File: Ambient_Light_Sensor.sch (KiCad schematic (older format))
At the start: 7 parts, among them U2001 OPT3001

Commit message: Resolved an issue with the field names of resistors on anode and grid driver sheets
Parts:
- R2004, R2005: value 100 -> 0
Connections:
- wire segments 6 -> 8
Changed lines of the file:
@@
 P 7230 3650
 F 0 "R2004" V 7630 3650 50  0000 C CNN
-F 1 "100" V 7230 3650 50  0000 C CNN
+F 1 "0" V 7230 3650 50  0000 C CNN
 F 2 "Resistors_SMD:R_0603" H 7230 3650 50  0001 C CNN
 F 3 "" H 7230 3650 50  0001 C CNN
@@
 P 7230 3750
 F 0 "R2005" V 7630 3750 50  0000 C CNN
-F 1 "100" V 7230 3750 50  0000 C CNN
+F 1 "0" V 7230 3750 50  0000 C CNN
 F 2 "Resistors_SMD:R_0603" H 7230 3750 50  0001 C CNN
 F 3 "" H 7230 3750 50  0001 C CNN
@@
 $EndComp
 Wire Wire Line
-	7080 3650 4450 3650
+	7080 3650 5640 3650
 Wire Wire Line
-	7080 3750 4450 3750
+	7080 3750 6260 3750
 $Comp
 L Custom-Library:+3.3V #PWR2003
@@
 	1    0    0    -1
 $EndComp
+Wire Wire Line
+	6260 3750 4450 3750
+Wire Wire Line
+	5640 3650 4450 3650
 $EndSCHEMATC

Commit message: Added a config field for every part, DNP some I2C pullups, added I2C header, changed some serial port functionality
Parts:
- R2002, R2003: Config (none) -> DNP
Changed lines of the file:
@@
 F 2 "Resistors_SMD:R_0603" H 6260 3350 50  0001 C CNN
 F 3 "" H 6260 3350 50  0001 C CNN
-F 4 "0603" H 6340 3430 50  0000 L CNN "display_footprint"
-F 5 "1%" H 6340 3350 50  0000 L CNN "Tolerance"
-F 6 "1/10W" H 6350 3270 50  0000 L CNN "Wattage"
-F 7 "A102203CT-ND" H 6560 3750 60  0001 C CNN "Digi-Key PN"
+F 4 "DNP" H 6340 3500 50  0000 L CNN "Config"
+F 5 "0603" H 6340 3430 50  0000 L CNN "display_footprint"
+F 6 "1%" H 6340 3350 50  0000 L CNN "Tolerance"
+F 7 "1/10W" H 6350 3270 50  0000 L CNN "Wattage"
+F 8 "A102203CT-ND" H 6560 3750 60  0001 C CNN "Digi-Key PN"
 	1    6260 3350
 	-1   0    0    -1
@@
 F 2 "Resistors_SMD:R_0603" H 5640 3350 50  0001 C CNN
 F 3 "" H 5640 3350 50  0001 C CNN
-F 4 "0603" H 5720 3430 50  0000 L CNN "display_footprint"
-F 5 "1%" H 5720 3350 50  0000 L CNN "Tolerance"
-F 6 "1/10W" H 5730 3270 50  0000 L CNN "Wattage"
-F 7 "A102203CT-ND" H 5940 3750 60  0001 C CNN "Digi-Key PN"
+F 4 "DNP" H 5720 3500 50  0000 L CNN "Config"
+F 5 "0603" H 5720 3430 50  0000 L CNN "display_footprint"
+F 6 "1%" H 5720 3350 50  0000 L CNN "Tolerance"
+F 7 "1/10W" H 5730 3270 50  0000 L CNN "Wattage"
+F 8 "A102203CT-ND" H 5940 3750 60  0001 C CNN "Digi-Key PN"
 	1    5640 3350
 	-1   0    0    -1

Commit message: Added I2C Address symbols for I2C devices
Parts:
- added A?: 0x44, symbol Custom_Library:I2C_Address
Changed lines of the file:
@@
 Wire Wire Line
 	5640 3650 4450 3650
+$Comp
+L Custom_Library:I2C_Address A?
+U 1 1 5B59CE96
+P 4070 4940
+F 0 "A?" H 4070 5190 60  0001 C CNN
+F 1 "0x44" H 3620 4940 60  0000 L CNN
+F 2 "" H 4070 5290 60  0001 C CNN
+F 3 "" H 4070 5290 60  0001 C CNN
+	1    4070 4940
+	1    0    0    -1
+$EndComp
 $EndSCHEMATC

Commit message: Annotated all components, finished assigning footprints, netlist generated
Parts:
- A2001: renamed from A?; footprint (none) -> Oddities:Dummy_Empty
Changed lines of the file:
@@
 $EndComp
 $Comp
-L power:GND #PWR2004
+L power:GND #PWR02004
 U 1 1 5AD7F5D1
 P 3600 4350
-F 0 "#PWR2004" H 3600 4100 50  0001 C CNN
+F 0 "#PWR02004" H 3600 4100 50  0001 C CNN
 F 1 "GND" H 3600 4200 50  0000 C CNN
 F 2 "" H 3600 4350 50  0001 C CNN
@@
 $EndComp
 $Comp
-L power:GND #PWR2005
+L power:GND #PWR02005
 U 1 1 5AD8750C
 P 4530 4430
-F 0 "#PWR2005" H 4530 4180 50  0001 C CNN
+F 0 "#PWR02005" H 4530 4180 50  0001 C CNN
 F 1 "GND" H 4530 4280 50  0000 C CNN
 F 2 "" H 4530 4430 50  0001 C CNN
@@
 	4530 4050 4450 4050
 $Comp
-L power:GND #PWR2002
+L power:GND #PWR02002
 U 1 1 5AEB7580
 P 2910 4890
-F 0 "#PWR2002" H 2910 4640 50  0001 C CNN
+F 0 "#PWR02002" H 2910 4640 50  0001 C CNN
 F 1 "GND" H 2910 4740 50  0000 C CNN
 F 2 "" H 2910 4890 50  0001 C CNN
@@
 	7080 3750 6260 3750
 $Comp
-L Custom-Library:+3.3V #PWR2003
+L Custom-Library:+3.3V #PWR02003
 U 1 1 5B3DF1B7
 P 3600 3350
-F 0 "#PWR2003" H 3600 3200 50  0001 C CNN
+F 0 "#PWR02003" H 3600 3200 50  0001 C CNN
 F 1 "+3.3V" H 3600 3490 50  0000 C CNN
 F 2 "" H 3600 3350 50  0000 C CNN
@@
 $EndComp
 $Comp
-L Custom-Library:+3.3V #PWR2001
+L Custom-Library:+3.3V #PWR02001
 U 1 1 5B3DF1EC
 P 2910 4590
-F 0 "#PWR2001" H 2910 4440 50  0001 C CNN
+F 0 "#PWR02001" H 2910 4440 50  0001 C CNN
 F 1 "+3.3V" H 2910 4730 50  0000 C CNN
 F 2 "" H 2910 4590 50  0000 C CNN
@@
 $EndComp
 $Comp
-L Custom-Library:+3.3V #PWR2006
+L Custom-Library:+3.3V #PWR02006
 U 1 1 5B3DF749
 P 5640 3200
-F 0 "#PWR2006" H 5640 3050 50  0001 C CNN
+F 0 "#PWR02006" H 5640 3050 50  0001 C CNN
 F 1 "+3.3V" H 5640 3340 50  0000 C CNN
 F 2 "" H 5640 3200 50  0000 C CNN
@@
 $EndComp
 $Comp
-L Custom-Library:+3.3V #PWR2007
+L Custom-Library:+3.3V #PWR02007
 U 1 1 5B3DF769
 P 6260 3200
-F 0 "#PWR2007" H 6260 3050 50  0001 C CNN
+F 0 "#PWR02007" H 6260 3050 50  0001 C CNN
 F 1 "+3.3V" H 6260 3340 50  0000 C CNN
 F 2 "" H 6260 3200 50  0000 C CNN
@@
 	5640 3650 4450 3650
 $Comp
-L Custom_Library:I2C_Address A?
+L Custom_Library:I2C_Address A2001
 U 1 1 5B59CE96
 P 4070 4940
-F 0 "A?" H 4070 5190 60  0001 C CNN
+F 0 "A2001" H 4070 5190 60  0001 C CNN
 F 1 "0x44" H 3620 4940 60  0000 L CNN
-F 2 "" H 4070 5290 60  0001 C CNN
+F 2 "Oddities:Dummy_Empty" H 4070 5290 60  0001 C CNN
 F 3 "" H 4070 5290 60  0001 C CNN
 	1    4070 4940

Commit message: Added a bunch of Digi-Key PN's
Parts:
- C2001: Digi-Key PN 478-9903-1-ND -> 399-6856-1-ND
- R2001, R2002, R2003: Digi-Key PN A102203CT-ND -> 541-10.0KHCT-ND
- R2004, R2005: Digi-Key PN P100HCT-ND -> P0.0GCT-ND
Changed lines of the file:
@@
 F 5 "1%" V 7430 3650 50  0000 C CNN "Tolerance"
 F 6 "1/10W" V 7530 3650 50  0000 C CNN "Wattage"
-F 7 "P100HCT-ND" H 7530 4050 60  0001 C CNN "Digi-Key PN"
+F 7 "P0.0GCT-ND" H 7530 4050 60  0001 C CNN "Digi-Key PN"
 	1    7230 3650
 	0    1    -1   0
@@
 F 5 "1%" V 7430 3750 50  0000 C CNN "Tolerance"
 F 6 "1/10W" V 7530 3750 50  0000 C CNN "Wattage"
-F 7 "P100HCT-ND" H 7530 4150 60  0001 C CNN "Digi-Key PN"
+F 7 "P0.0GCT-ND" H 7530 4150 60  0001 C CNN "Digi-Key PN"
 	1    7230 3750
 	0    -1   1    0
@@
 F 6 "1%" H 6340 3350 50  0000 L CNN "Tolerance"
 F 7 "1/10W" H 6350 3270 50  0000 L CNN "Wattage"
-F 8 "A102203CT-ND" H 6560 3750 60  0001 C CNN "Digi-Key PN"
+F 8 "541-10.0KHCT-ND" H 6560 3750 60  0001 C CNN "Digi-Key PN"
 	1    6260 3350
 	-1   0    0    -1
@@
 F 6 "1%" H 5720 3350 50  0000 L CNN "Tolerance"
 F 7 "1/10W" H 5730 3270 50  0000 L CNN "Wattage"
-F 8 "A102203CT-ND" H 5940 3750 60  0001 C CNN "Digi-Key PN"
+F 8 "541-10.0KHCT-ND" H 5940 3750 60  0001 C CNN "Digi-Key PN"
 	1    5640 3350
 	-1   0    0    -1
@@
 F 5 "1%" H 4610 4280 50  0000 L CNN "Tolerance"
 F 6 "1/10W" H 4610 4200 50  0000 L CNN "Wattage"
-F 7 "A102203CT-ND" H 4830 4680 60  0001 C CNN "Digi-Key PN"
+F 7 "541-10.0KHCT-ND" H 4830 4680 60  0001 C CNN "Digi-Key PN"
 	1    4530 4280
 	1    0    0    -1
@@
 F 5 "50V" H 2760 4740 50  0000 R CNN "Voltage"
 F 6 "X7R" H 2760 4640 50  0000 R CNN "Dielectric"
-F 7 "478-9903-1-ND" H 2910 4740 60  0001 C CNN "Digi-Key PN"
+F 7 "399-6856-1-ND" H 2910 4740 60  0001 C CNN "Digi-Key PN"
 	1    2910 4740
 	1    0    0    -1

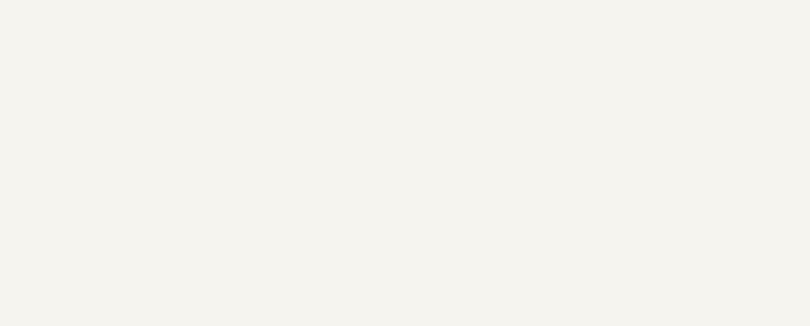
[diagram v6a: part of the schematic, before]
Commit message: Arranged more components on PCB, cleaned up schematic, added page titles, finished finding DigiKey PN's
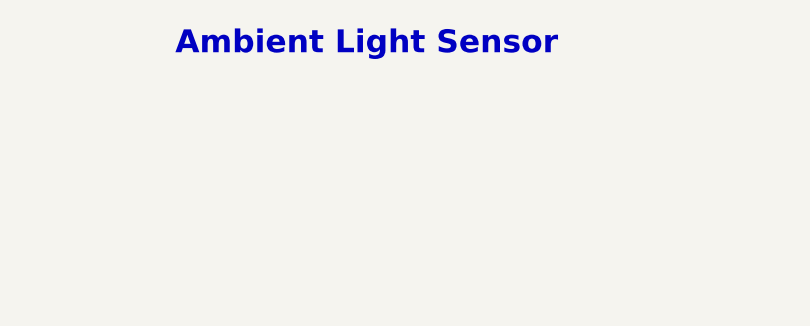
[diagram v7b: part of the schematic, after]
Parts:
- R2001: Digi-Key PN 541-10.0KHCT-ND -> P10.0KHCT-ND
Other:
- note added: "Ambient Light Sensor"
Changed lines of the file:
@@
 F 5 "1%" H 4610 4280 50  0000 L CNN "Tolerance"
 F 6 "1/10W" H 4610 4200 50  0000 L CNN "Wattage"
-F 7 "541-10.0KHCT-ND" H 4830 4680 60  0001 C CNN "Digi-Key PN"
+F 7 "P10.0KHCT-ND" H 4830 4680 60  0001 C CNN "Digi-Key PN"
 	1    4530 4280
 	1    0    0    -1
@@
 	1    0    0    -1
 $EndComp
+Text Notes 4090 980  0    100  ~ 20
+Ambient Light Sensor
 $EndSCHEMATC
